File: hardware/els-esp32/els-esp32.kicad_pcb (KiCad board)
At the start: 2 copper layers, 76.3 x 49.6 mm, 63 parts, among them J1 USB B Micro, J2 Rotary Encoder, J3 LED Display, J4 Stepper Driver/Servo, J5 Power, J6 Expansion, Q1 2N7002, Q10 2N7002, Q11 2N7002, Q2 2N7002, Q3 2N7002, Q4 2N7002, Q5 2N7002, Q6 2N7002, Q7 MMBT3904, Q8 MMBT3904, Q9 2N7002, SW1 Reset, U1 AMS1117-3.3, U2 CP2104, U3 ESP32-WROOM-32

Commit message: minor layout
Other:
- board text added: ""Adding IoT vulnerabilities to an old lathe is the perfect way to bring it into the 21st century" - Mark Twain (allegedly)"
- board text removed: "Bringing IoT vulnerability to a old lathe"
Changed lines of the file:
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@@
       (layerselection 0x010fc_ffffffff)
       (usegerberextensions true)
-      (usegerberattributes true)
+      (usegerberattributes false)
       (usegerberadvancedattributes false)
       (creategerberjobfile false)
@@
     )
   )
-  (gr_text "Bringing IoT vulnerability to a old lathe" (at 130.175 61.468) (layer B.SilkS)
-    (effects (font (size 1 1) (thickness 0.15)) (justify mirror))
+  (gr_text "\"Adding IoT vulnerabilities to an old lathe is the perfect way to bring it into the 21st century\" - Mark Twain (allegedly)" (at 130.556 95.377) (layer B.SilkS)
+    (effects (font (size 1 0.6) (thickness 0.1)) (justify mirror))
   )
   (gr_text JLCJLCJLCJLC (at 105.918 95.631) (layer F.SilkS)
@@
   (segment (start 147.079 61.976) (end 149.196 61.976) (width 0.5) (layer F.Cu) (net 3) (status 10))
   (segment (start 151.384 59.538) (end 151.384 53.238) (width 0.5) (layer F.Cu) (net 3) (status 30))
-  (segment (start 123.698 62.992) (end 141.732 62.992) (width 0.5) (layer B.Cu) (net 3))
   (segment (start 104.46 61.926) (end 104.41 61.976) (width 0.5) (layer F.Cu) (net 3) (status 30))
   (segment (start 104.46 59.928) (end 104.46 61.926) (width 0.5) (layer F.Cu) (net 3) (status 30))
@@
   (segment (start 124.523 86.677) (end 124.968 87.122) (width 0.5) (layer F.Cu) (net 3))
   (segment (start 123.317 86.677) (end 124.523 86.677) (width 0.5) (layer F.Cu) (net 3) (status 10))
+  (segment (start 123.698 62.992) (end 141.732 62.992) (width 0.5) (layer B.Cu) (net 3))
   (segment (start 127.602 83.024) (end 127.602 84.074) (width 0.25) (layer F.Cu) (net 4) (status 20))
   (segment (start 127.602 83.024) (end 127.677001 82.948999) (width 0.25) (layer F.Cu) (net 4))

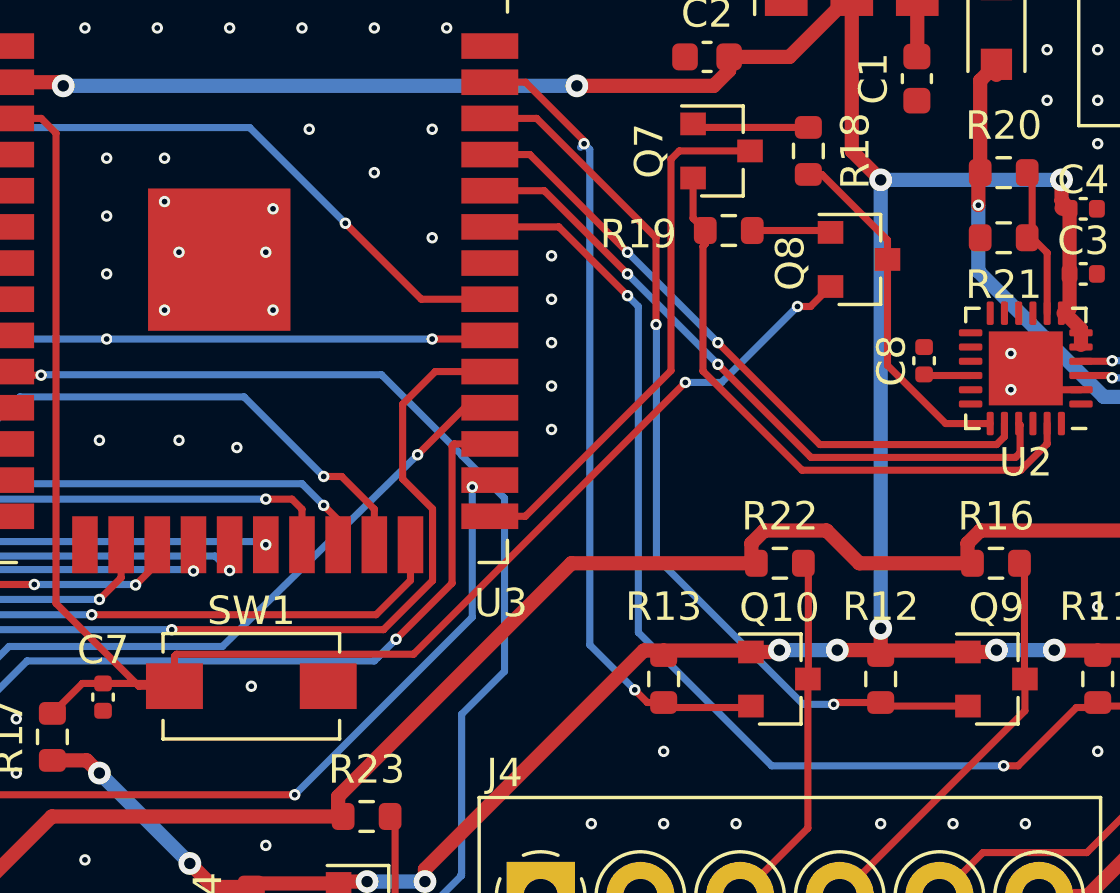
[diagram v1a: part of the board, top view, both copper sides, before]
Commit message: Fixed hardware bug, one transistor was reversed
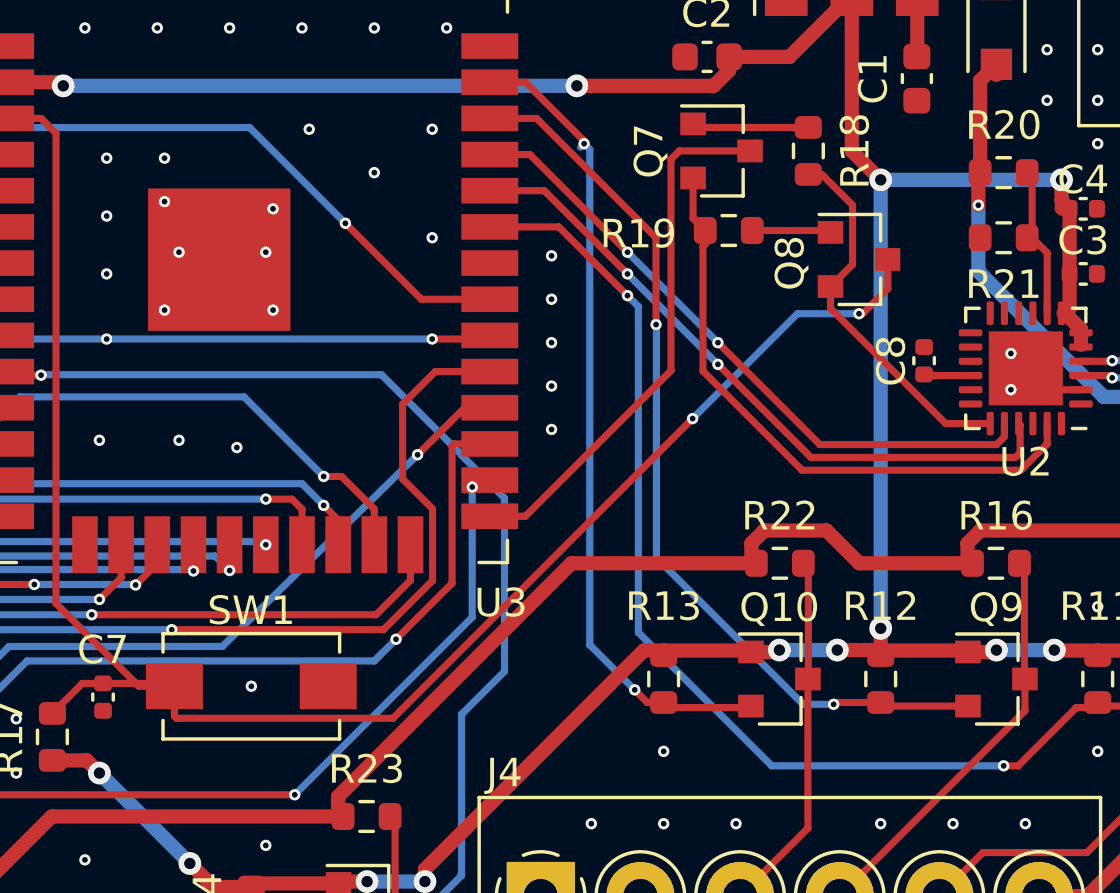
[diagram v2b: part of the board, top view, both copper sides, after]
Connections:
- Q8 pad 2: RESET -> RTS
- Q8 pad 3: RTS -> RESET
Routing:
- net RESET: track 58.1 -> 62.0 mm
- net RTS: track 12.6 -> 13.2 mm
